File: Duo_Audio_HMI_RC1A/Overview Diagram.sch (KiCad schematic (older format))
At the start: 0 parts

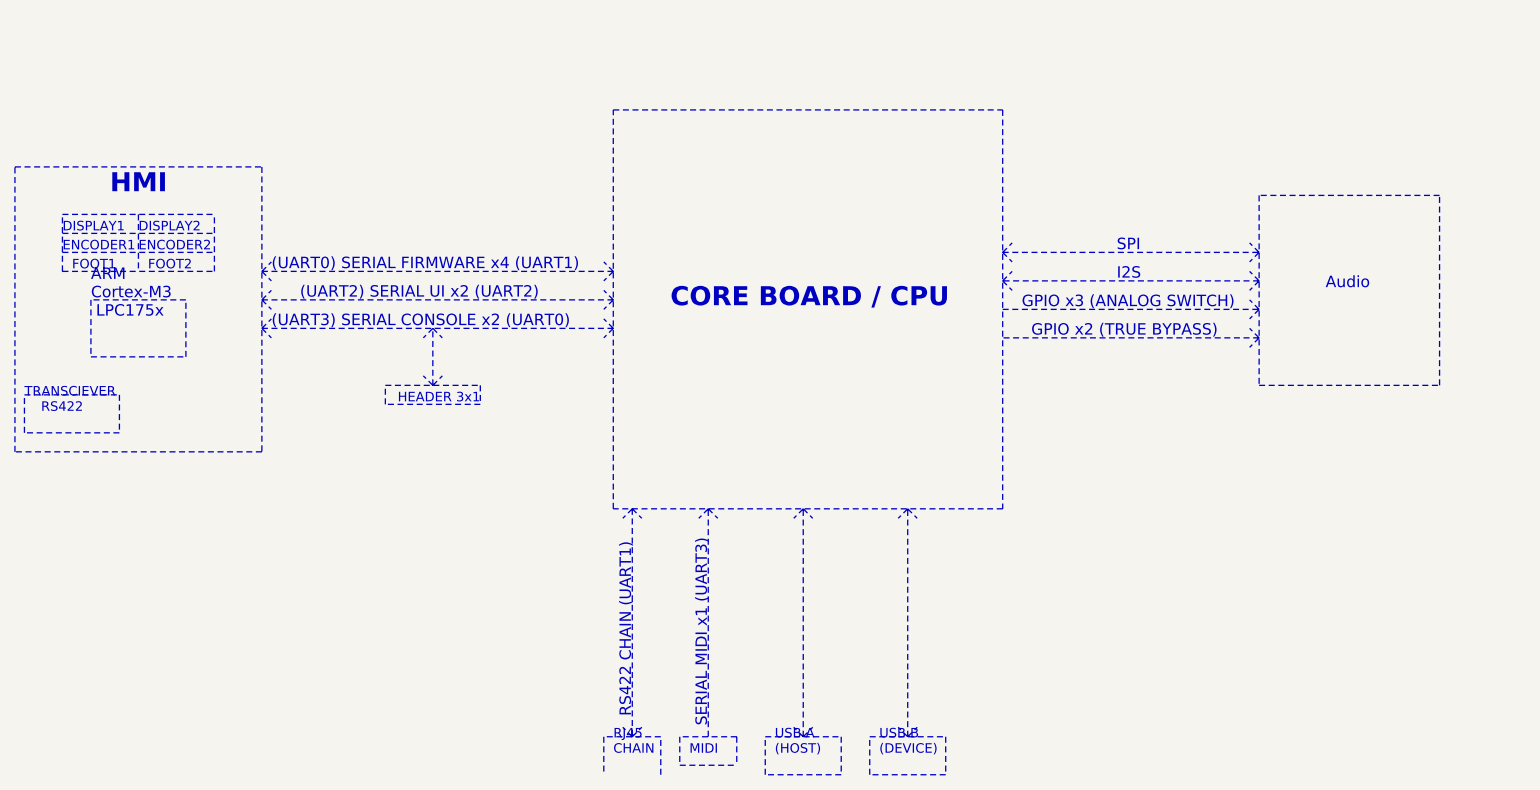
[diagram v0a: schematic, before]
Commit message: Implementing RCA1 schematic  modifications for new layout. Backup commit.
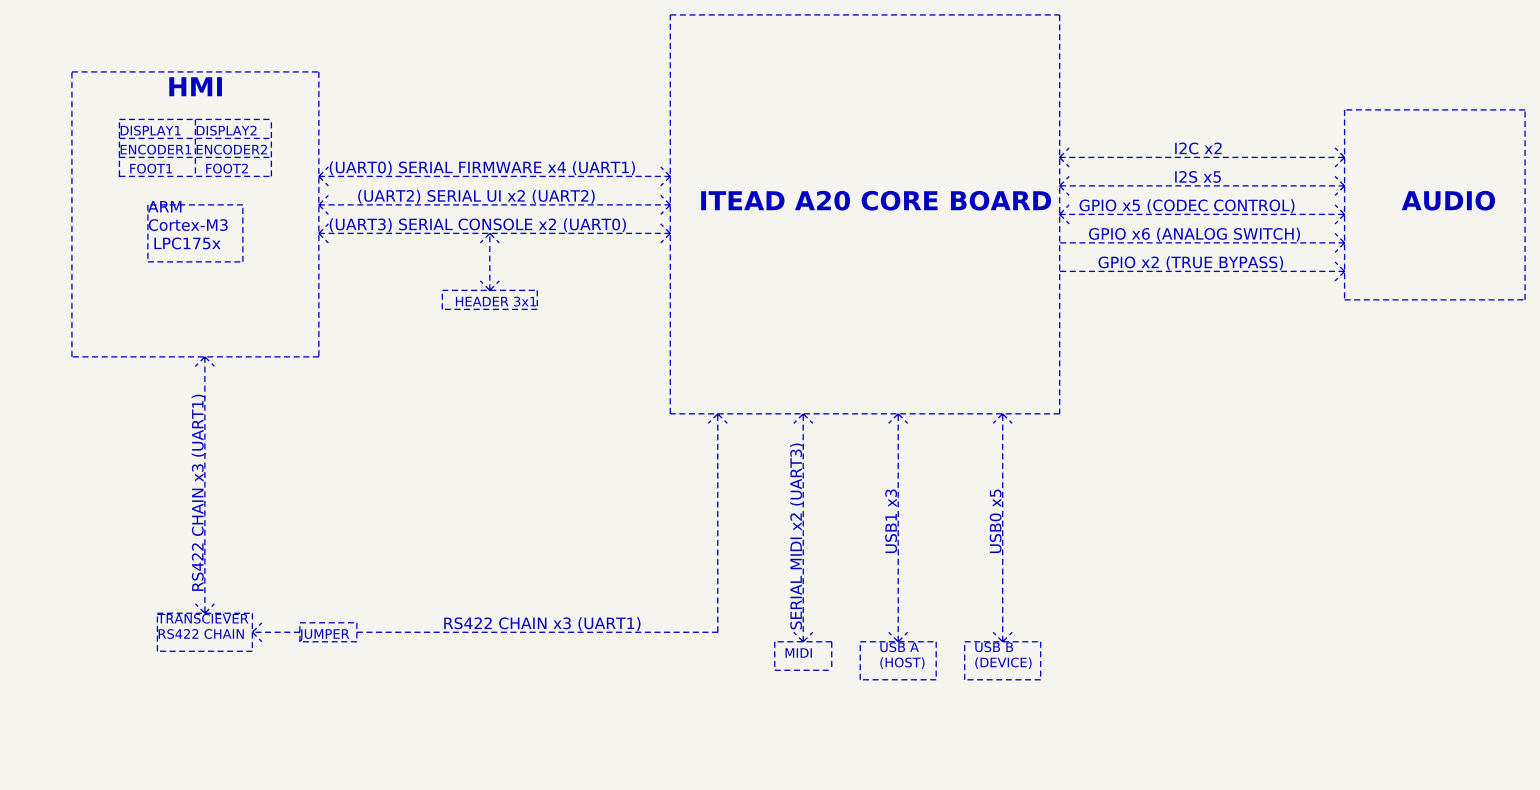
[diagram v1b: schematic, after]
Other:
- note added: "AUDIO"
- note added: "GPIO x5 (CODEC CONTROL)"
- note added: "GPIO x6 (ANALOG SWITCH)"
- note added: "I2C x2"
- note added: "I2S x5"
- note added: "ITEAD A20 CORE BOARD"
- note added: "JUMPER"
- note added: "RS422 CHAIN x3 (UART1)"
- note added: "SERIAL MIDI x2 (UART3)"
- note added: "TRANSCIEVER\nRS422 CHAIN"
- note added: "USB0 x5"
- note added: "USB1 x3"
- note removed: "Audio"
- note removed: "CORE BOARD / CPU"
- note removed: "GPIO x3 (ANALOG SWITCH)"
- note removed: "I2S"
- note removed: "RJ45 \nCHAIN"
- note removed: "RS422 CHAIN (UART1)"
- note removed: "SERIAL MIDI x1 (UART3)"
- note removed: "SPI"
- note removed: "TRANSCIEVER\n RS422"

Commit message: Finished RCA1 schematic of the Baseboard and the Pannelboard with USB OTG. Board dimensions, most footprint attribution and major placement implemented in layout. Learning GIT!
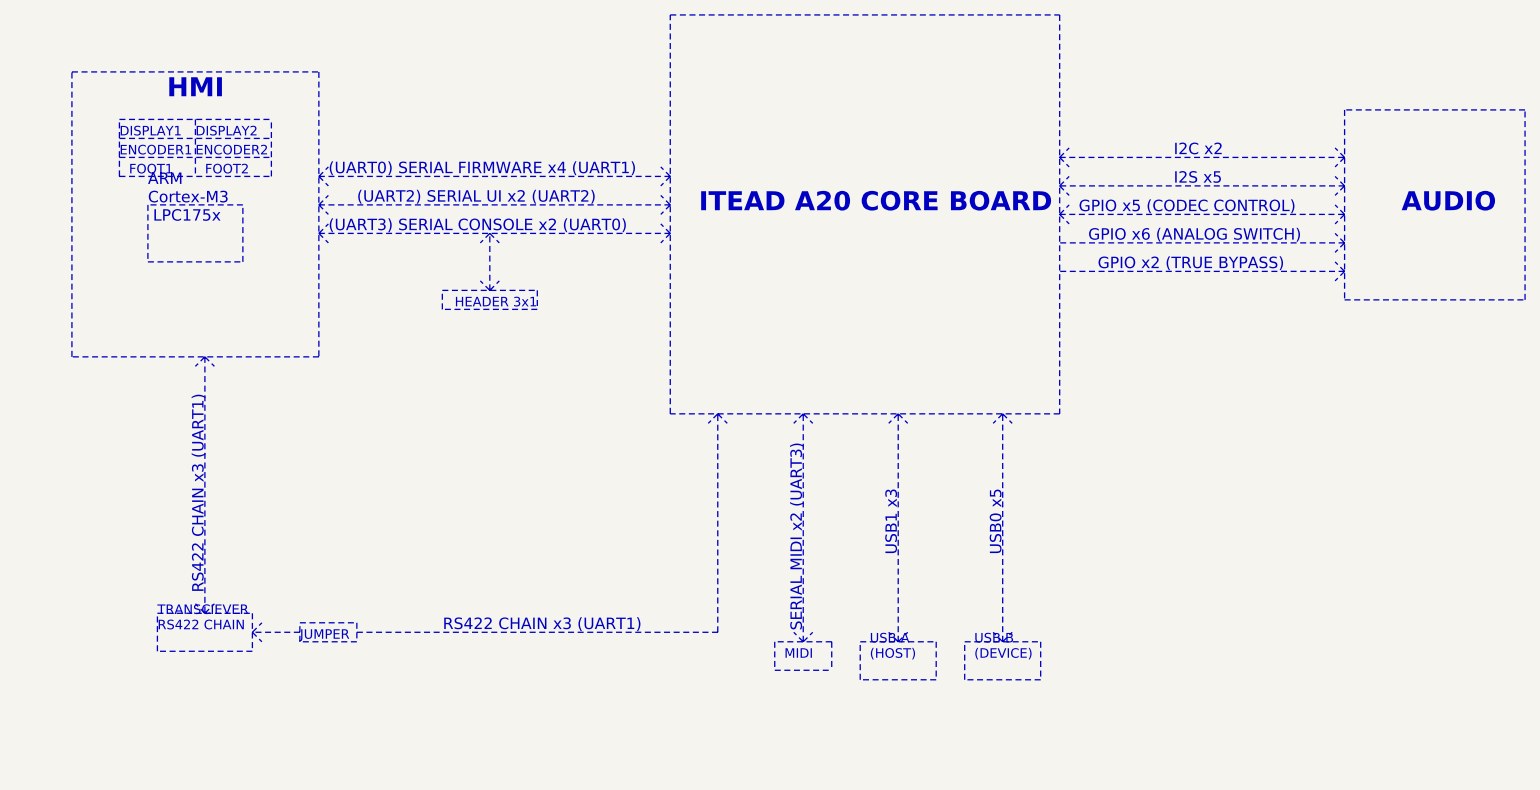
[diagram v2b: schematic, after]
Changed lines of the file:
@@
 LIBS:Duo_Audio_HMI_RC1A
 LIBS:Duo_Audio_HMI_RC1A-cache
-EELAYER 24 0
+EELAYER 27 0
 EELAYER END
 $Descr A4 11693 8268
@@
 Sheet 2 10
 Title "MOD Duo Baseboard RC1A"
-Date "14 may 2014"
+Date "20 may 2014"
 Rev "RC1A"
 Comp ""
@@
 Text Notes 5400 3250 0    100  ~ 20
 ITEAD A20 CORE BOARD
-Text Notes 2500 3450 0    60   ~ 0
+Text Notes 2500 3300 0    60   ~ 0
    ARM \nCortex-M3\n LPC175x
 Text Notes 7900 3100 0    60   ~ 0
@@
 Text Notes 2600 2650 0    100  ~ 20
 HMI
-Text Notes 2550 5500 0    50   ~ 0
+Text Notes 2550 5450 0    50   ~ 0
 TRANSCIEVER\nRS422 CHAIN
 Wire Notes Line
@@
 Wire Notes Line
 	3000 3500 3000 3200
-Text Notes 6350 5650 0    50   ~ 0
+Text Notes 6300 5600 0    50   ~ 0
 USB A\n(HOST)\n
-Text Notes 6850 5650 0    50   ~ 0
+Text Notes 6850 5600 0    50   ~ 0
  USB B\n(DEVICE)\n
 Wire Notes Line
